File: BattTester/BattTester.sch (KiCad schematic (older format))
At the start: 35 parts, among them J1 Battery, J2 SD_Card, J3 PWR, J4 UPDI, Q1 IRLZ44N, Q2 IRF4905, Q3 2N7002, U1 LTC1286CN8, U2 ATtiny1624-SS, U3 LM1117-3.3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

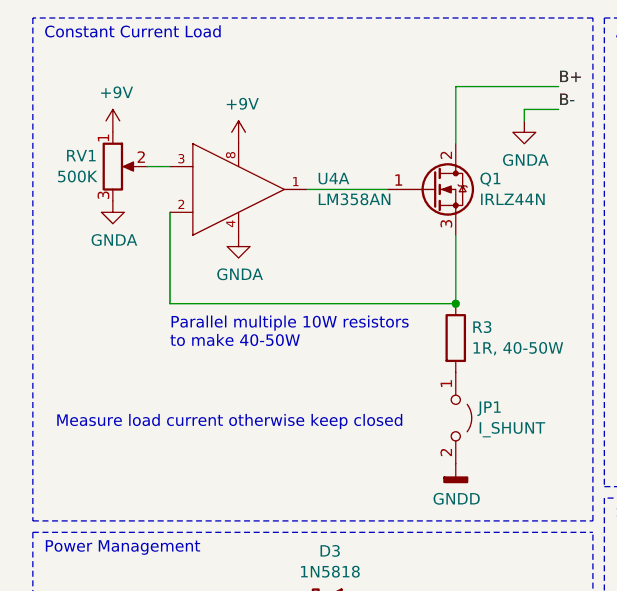
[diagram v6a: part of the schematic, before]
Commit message: standardize dip-8, tie off second lm358 output
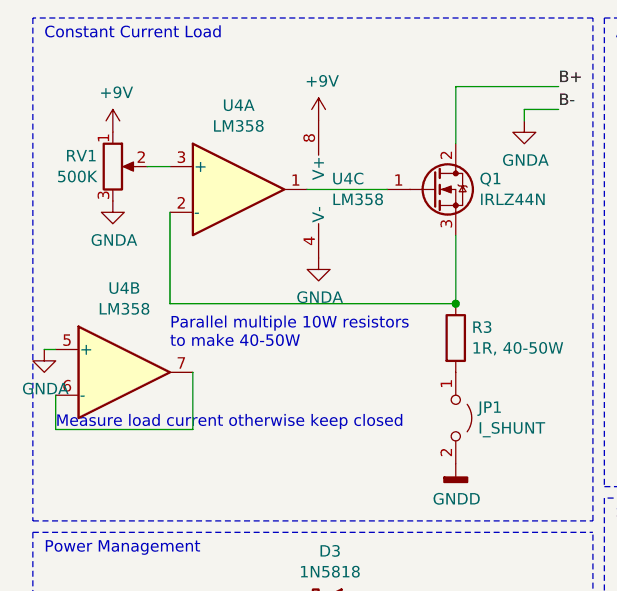
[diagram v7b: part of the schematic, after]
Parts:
- removed U4: LM358AN, BattTester:DIP8, symbol LM358AN:LM358AN_NOPB
- added U4: LM358, Package_DIP:DIP-8_W7.62mm_Socket, symbol Amplifier_Operational:LM358
- U1: footprint BattTester:DIP8 -> Package_DIP:DIP-8_W7.62mm_Socket
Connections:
- net +9V: now also U4.8 (V+)
- net GND: now also U4.4 (V-), U4.5 (+)
- net at RV1.2: now also U4.3 (+)
- net at Q1.1 (G): now also U4.1
- net at Q1.3 (S), R3.1: now also U4.2 (-)
- new net: U4.6 (-), U4.7
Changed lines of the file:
@@
 	1700 1250 2050 1250
-$Comp
-L LM358AN:LM358AN_NOPB U4
-U 1 1 6172AB33
-P 1100 1150
-F 0 "U4" H 1744 1096 50  0000 L CNN
-F 1 "LM358AN" H 1744 1005 50  0000 L CNN
-F 2 "BattTester:DIP8" H 1100 1550 50  0001 L CNN
-F 3 "http://www.ti.com/lit/ds/symlink/lm358-n.pdf" H 1100 1650 50  0001 L CNN
-F 4 "No" H 1100 1750 50  0001 L CNN "automotive"
-F 5 "IC" H 1100 1850 50  0001 L CNN "category"
-F 6 "Integrated Circuits (ICs)" H 1100 1950 50  0001 L CNN "device class L1"
-F 7 "Linear ICs" H 1100 2050 50  0001 L CNN "device class L2"
-F 8 "Amplifiers - Op Amps" H 1100 2150 50  0001 L CNN "device class L3"
-F 9 "IC OPAMP GP 2 CIRCUIT 8DIP" H 1100 2250 50  0001 L CNN "digikey description"
-F 10 "LM358ANNS/NOPB-ND" H 1100 2350 50  0001 L CNN "digikey part number"
-F 11 "1MHz" H 1100 2450 50  0001 L CNN "gain bandwidth"
-F 12 "5.08mm" H 1100 2550 50  0001 L CNN "height"
-F 13 "0.045uA" H 1100 2650 50  0001 L CNN "input bias current"
-F 14 "2mV" H 1100 2750 50  0001 L CNN "input offset voltage"
-F 15 "DIP794W46P254L1016H508Q8" H 1100 2850 50  0001 L CNN "ipc land pattern name"
-F 16 "Yes" H 1100 2950 50  0001 L CNN "lead free"
-F 17 "14e3c34b0210167e" H 1100 3050 50  0001 L CNN "library id"
-F 18 "Texas Instruments" H 1100 3150 50  0001 L CNN "manufacturer"
-F 19 "16V" H 1100 3250 50  0001 L CNN "max dual supply voltage"
-F 20 "32V" H 1100 3350 50  0001 L CNN "max supply voltage"
-F 21 "1.5V" H 1100 3450 50  0001 L CNN "min dual supply voltage"
-F 22 "3V" H 1100 3550 50  0001 L CNN "min supply voltage"
-F 23 "Operational Amplifiers - Op Amps LOW PWR DUAL OP AMP\\n" H 1100 3650 50  0001 L CNN "mouser description"
-F 24 "926-LM358AN/NOPB" H 1100 3750 50  0001 L CNN "mouser part number"
-F 25 "0.5-1mA" H 1100 3850 50  0001 L CNN "nominal supply current"
-F 26 "2" H 1100 3950 50  0001 L CNN "number of channels"
-F 27 "20mA" H 1100 4050 50  0001 L CNN "output current per channel"
-F 28 "DIP8" H 1100 4150 50  0001 L CNN "package"
-F 29 "Yes" H 1100 4250 50  0001 L CNN "rohs"
-F 30 "0.51mm" H 1100 4350 50  0001 L CNN "standoff height"
-F 31 "+70°C" H 1100 4450 50  0001 L CNN "temperature range high"
-F 32 "0°C" H 1100 4550 50  0001 L CNN "temperature range low"
-F 33 "100V/mV" H 1100 4650 50  0001 L CNN "voltage gain"
-	1    1100 1150
-	1    0    0    -1
-$EndComp
 $Comp
 L power:GNDA #PWR0121
 U 1 1 617306EB
-P 1400 1450
-F 0 "#PWR0121" H 1400 1200 50  0001 C CNN
-F 1 "GNDA" H 1405 1277 50  0000 C CNN
-F 2 "" H 1400 1450 50  0001 C CNN
-F 3 "" H 1400 1450 50  0001 C CNN
-	1    1400 1450
+P 1750 1550
+F 0 "#PWR0121" H 1750 1300 50  0001 C CNN
+F 1 "GNDA" H 1755 1377 50  0000 C CNN
+F 2 "" H 1750 1550 50  0001 C CNN
+F 3 "" H 1750 1550 50  0001 C CNN
+	1    1750 1550
 	1    0    0    -1
 $EndComp
@@
 F 0 "U1" H 4625 1525 50  0000 C CNN
 F 1 "LTC1286CN8" H 4625 1434 50  0000 C CNN
-F 2 "BattTester:DIP8" H 4650 1450 50  0001 C CNN
+F 2 "Package_DIP:DIP-8_W7.62mm_Socket" H 4650 1450 50  0001 C CNN
 F 3 "" H 4650 1450 50  0001 C CNN
 	1    4650 1450
@@
 L power:+9V #PWR0120
 U 1 1 616CDCCB
-P 1400 1050
-F 0 "#PWR0120" H 1400 900 50  0001 C CNN
-F 1 "+9V" H 1415 1223 50  0000 C CNN
-F 2 "" H 1400 1050 50  0001 C CNN
-F 3 "" H 1400 1050 50  0001 C CNN
-	1    1400 1050
+P 1750 950
+F 0 "#PWR0120" H 1750 800 50  0001 C CNN
+F 1 "+9V" H 1765 1123 50  0000 C CNN
+F 2 "" H 1750 950 50  0001 C CNN
+F 3 "" H 1750 950 50  0001 C CNN
+	1    1750 950
 	1    0    0    -1
 $EndComp
@@
 	8100 3800 8100 3700
 Connection ~ 8100 3700
+$Comp
+L Amplifier_Operational:LM358 U4
+U 1 1 61A1DDF7
+P 1400 1250
+F 0 "U4" H 1400 1617 50  0000 C CNN
+F 1 "LM358" H 1400 1526 50  0000 C CNN
+F 2 "Package_DIP:DIP-8_W7.62mm_Socket" H 1400 1250 50  0001 C CNN
+F 3 "http://www.ti.com/lit/ds/symlink/lm2904-n.pdf" H 1400 1250 50  0001 C CNN
+	1    1400 1250
+	1    0    0    -1
+$EndComp
+$Comp
+L Amplifier_Operational:LM358 U4
+U 2 1 61A2D42F
+P 900 2050
+F 0 "U4" H 900 2417 50  0000 C CNN
+F 1 "LM358" H 900 2326 50  0000 C CNN
+F 2 "Package_DIP:DIP-8_W7.62mm_Socket" H 900 2050 50  0001 C CNN
+F 3 "http://www.ti.com/lit/ds/symlink/lm2904-n.pdf" H 900 2050 50  0001 C CNN
+	2    900  2050
+	1    0    0    -1
+$EndComp
+$Comp
+L Amplifier_Operational:LM358 U4
+U 3 1 61A31D94
+P 1850 1250
+F 0 "U4" H 1808 1296 50  0000 L CNN
+F 1 "LM358" H 1808 1205 50  0000 L CNN
+F 2 "Package_DIP:DIP-8_W7.62mm_Socket" H 1850 1250 50  0001 C CNN
+F 3 "http://www.ti.com/lit/ds/symlink/lm2904-n.pdf" H 1850 1250 50  0001 C CNN
+	3    1850 1250
+	1    0    0    -1
+$EndComp
+Wire Wire Line
+	1200 2050 1200 2300
+Wire Wire Line
+	1200 2300 600  2300
+Wire Wire Line
+	600  2300 600  2150
+$Comp
+L power:GNDA #PWR0127
+U 1 1 61A41730
+P 550 1950
+F 0 "#PWR0127" H 550 1700 50  0001 C CNN
+F 1 "GNDA" H 555 1777 50  0000 C CNN
+F 2 "" H 550 1950 50  0001 C CNN
+F 3 "" H 550 1950 50  0001 C CNN
+	1    550  1950
+	1    0    0    -1
+$EndComp
+Wire Wire Line
+	550  1950 600  1950
 $EndSCHEMATC
